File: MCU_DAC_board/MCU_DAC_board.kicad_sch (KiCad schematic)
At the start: 46 parts, among them J10 Conn_01x03_Pin, J11 105-0752-001, J12 Conn_02x03_Odd_Even, J5 54-00127, J6 105-0752-001, J7 Screw_Terminal_01x02, J8 Screw_Terminal_01x02, J9 Conn_02x20_Odd_Even, Q1 FZT953, U1 ADAU1966AWBSTZ

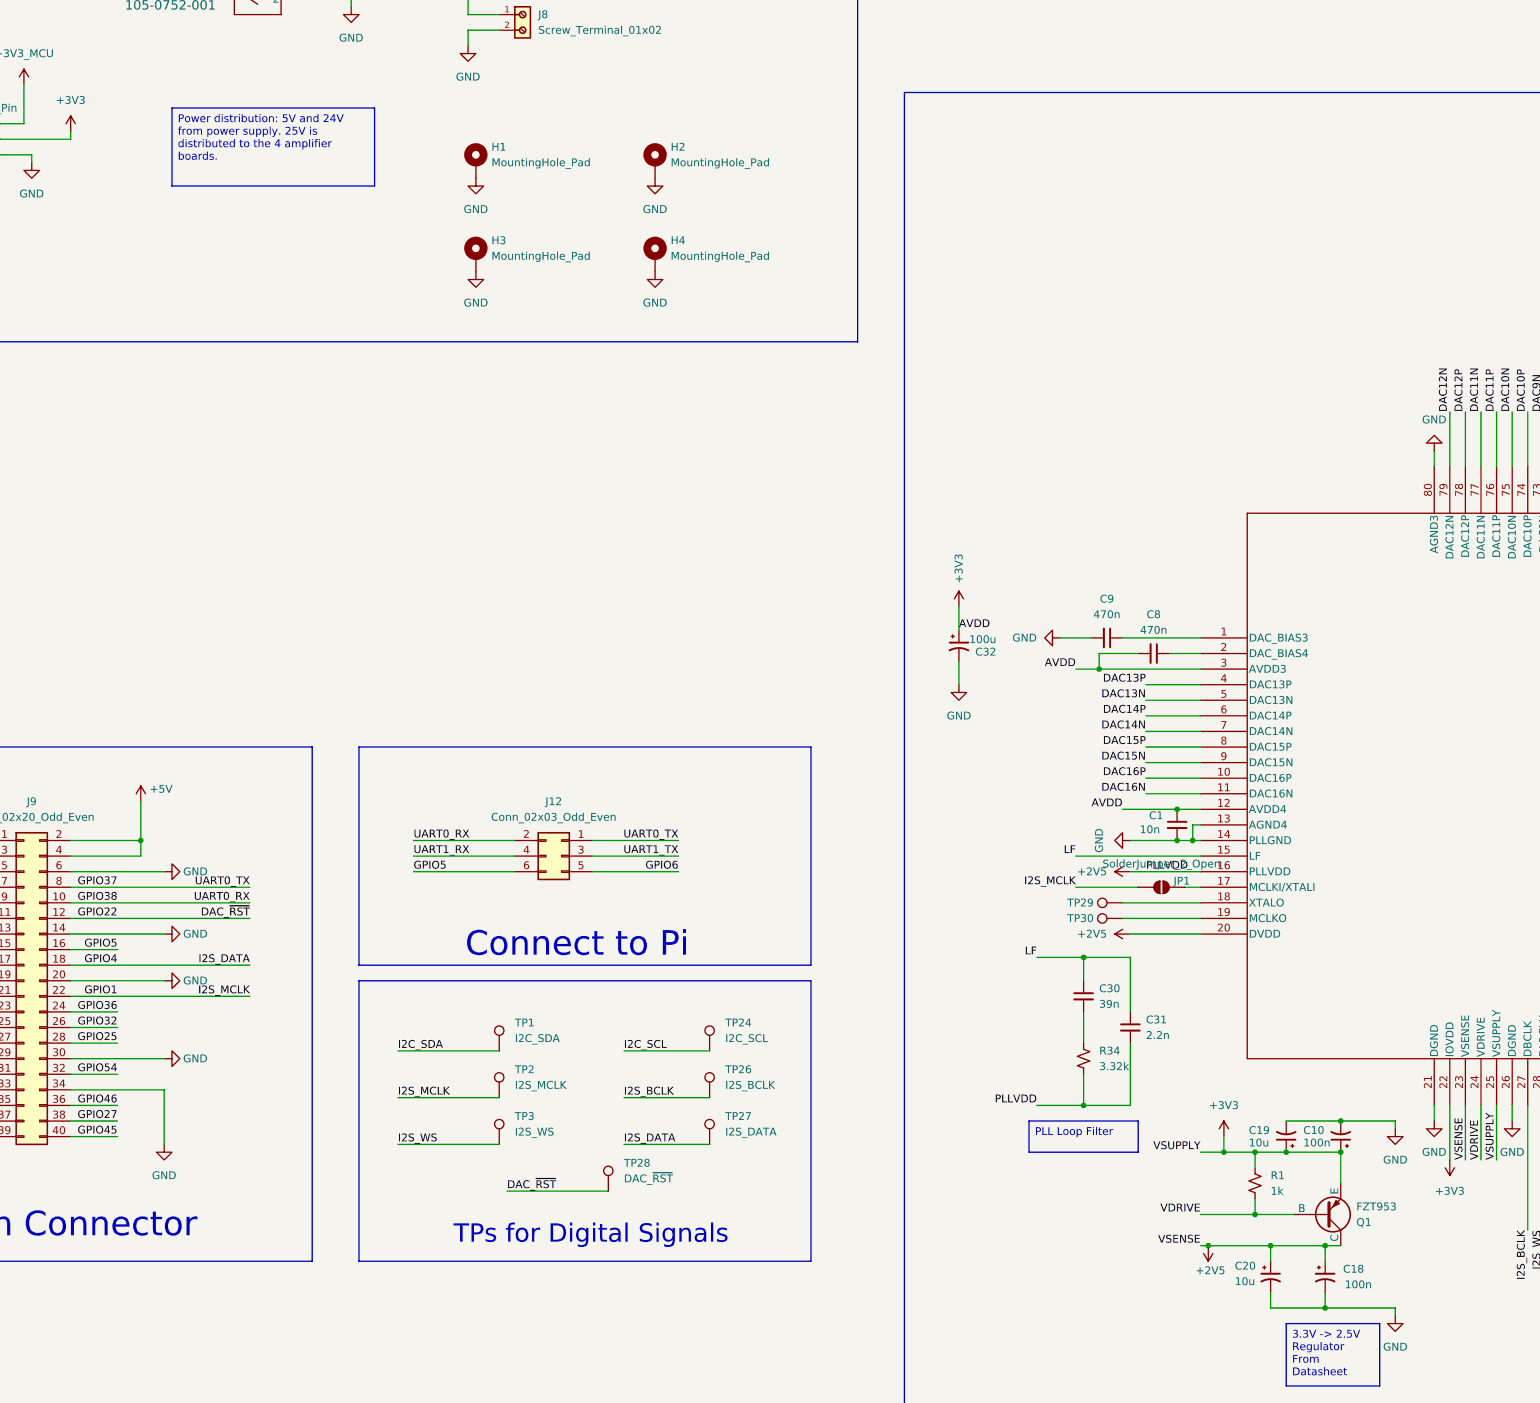
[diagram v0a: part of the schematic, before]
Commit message: First revision of DAC board
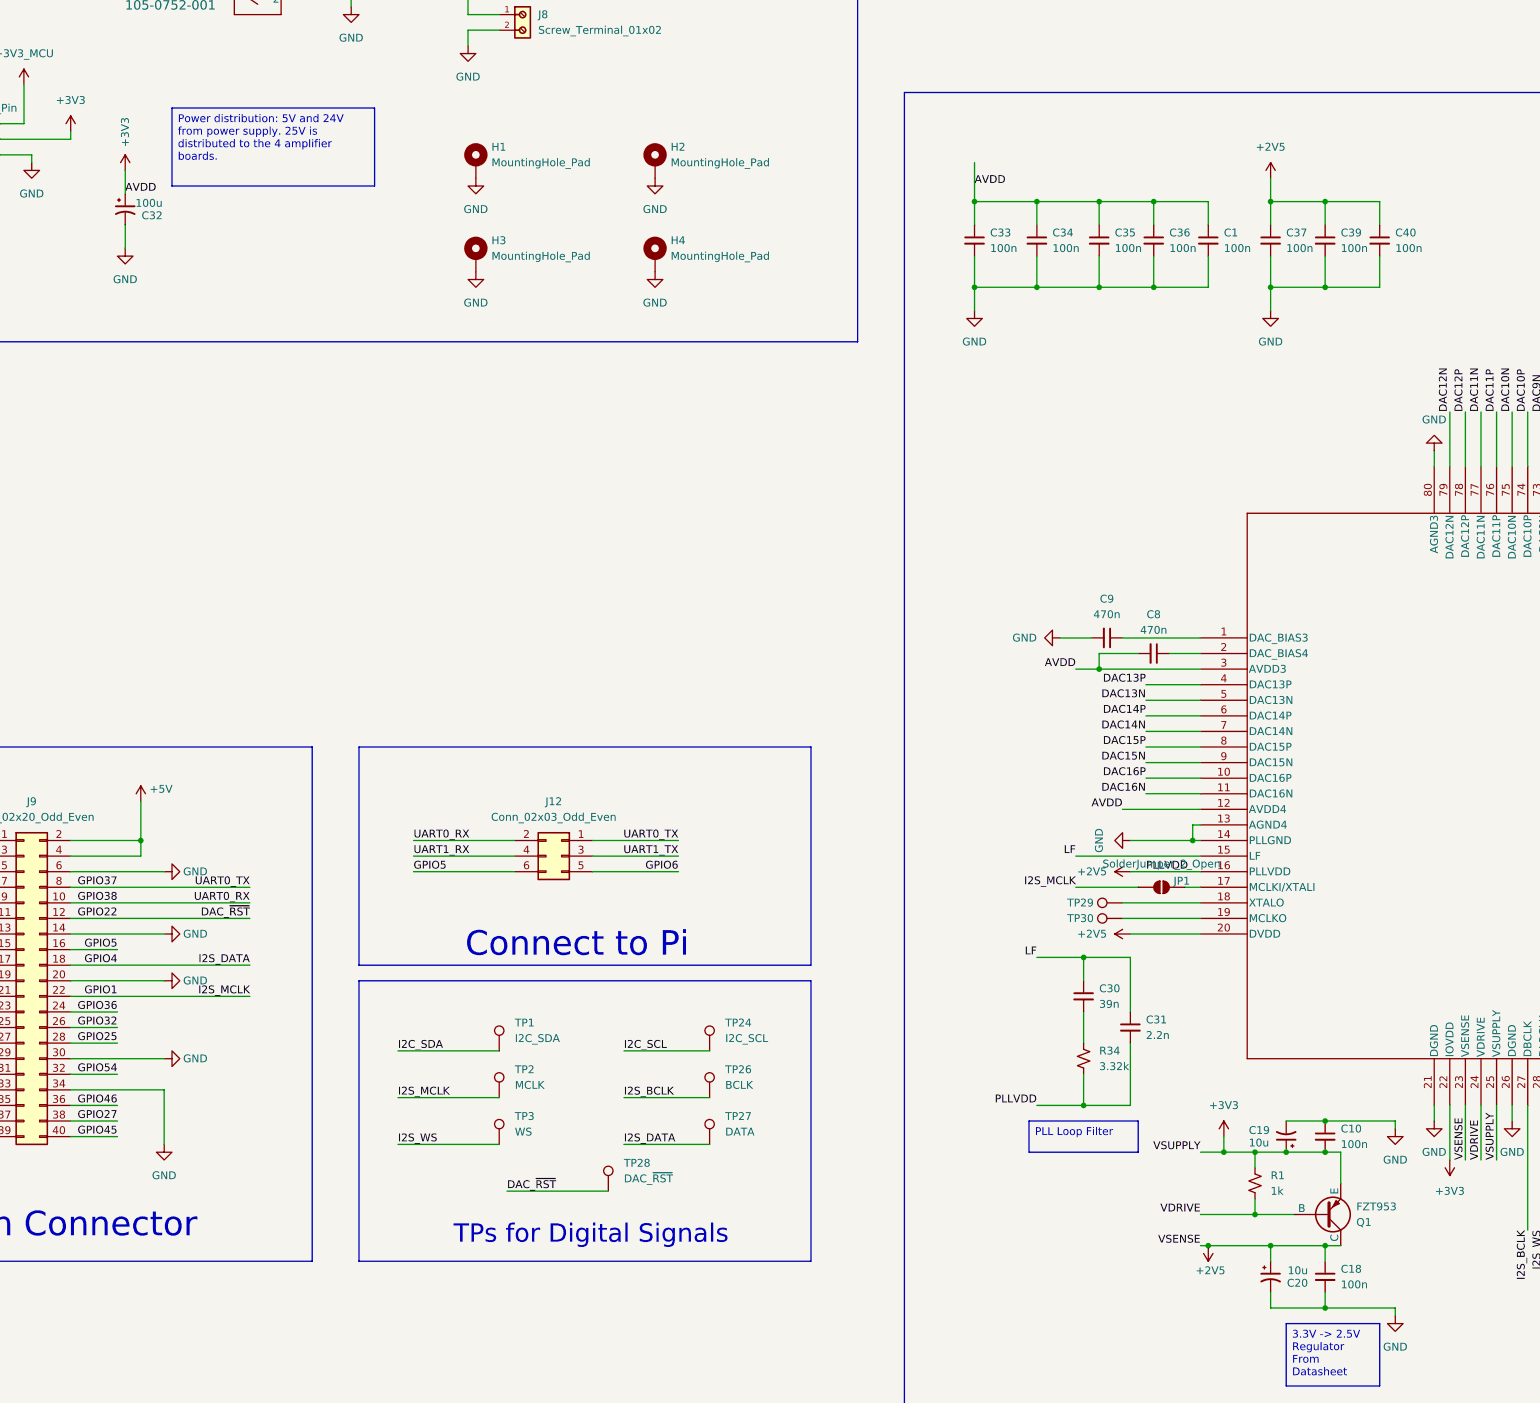
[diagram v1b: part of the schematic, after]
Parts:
- removed C10, C18: 100n, Capacitor_SMD:C_0805_2012Metric_Pad1.18x1.45mm_HandSolder, symbol Device:C_Polarized_Small_US
- added C10, C18, C33, C34, C35, C36, C37, C39, C40: 100n, Capacitor_SMD:C_0603_1608Metric_Pad1.08x0.95mm_HandSolder, symbol Device:C_Small
- C1: value 10n -> 100n; footprint Capacitor_SMD:C_0805_2012Metric_Pad1.18x1.45mm_HandSolder -> Capacitor_SMD:C_0603_1608Metric_Pad1.08x0.95mm_HandSolder
- C19, C20: footprint Capacitor_SMD:C_0805_2012Metric_Pad1.18x1.45mm_HandSolder -> Capacitor_SMD:CP_Elec_4x4.5
- C2, C3, C4, C7, C8, C9: footprint Capacitor_SMD:C_0805_2012Metric_Pad1.18x1.45mm_HandSolder -> Capacitor_SMD:C_0603_1608Metric_Pad1.08x0.95mm_HandSolder
- TP2: value I2S_MCLK -> MCLK
- TP26: value I2S_BCLK -> BCLK
- TP27: value I2S_DATA -> DATA
- TP3: value I2S_WS -> WS
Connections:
- net +2V5: now also C18.1, C37.1, C39.1, C40.1
- net +3V3: now also C10.2, C33.1, C34.1, C35.1, C36.1
- net GND: now also C10.1, C18.2, C33.2, C34.2, C35.2, C36.2, C37.2, C39.2, C40.2
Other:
- moved on the sheet: C32

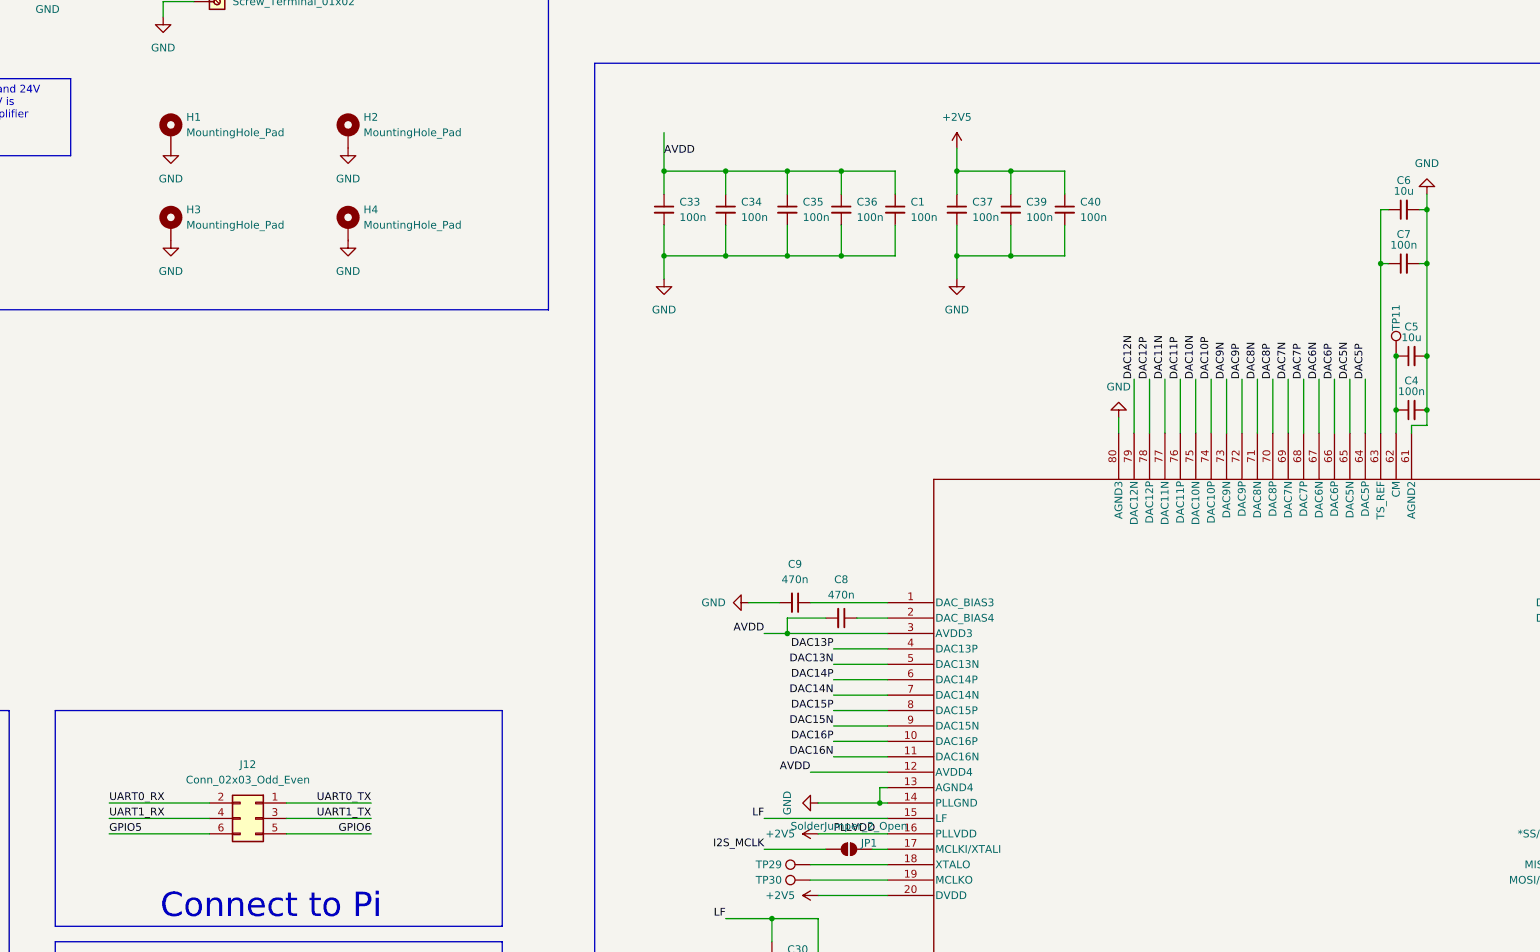
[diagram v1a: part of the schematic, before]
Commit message: Added via stiching, more decoupling
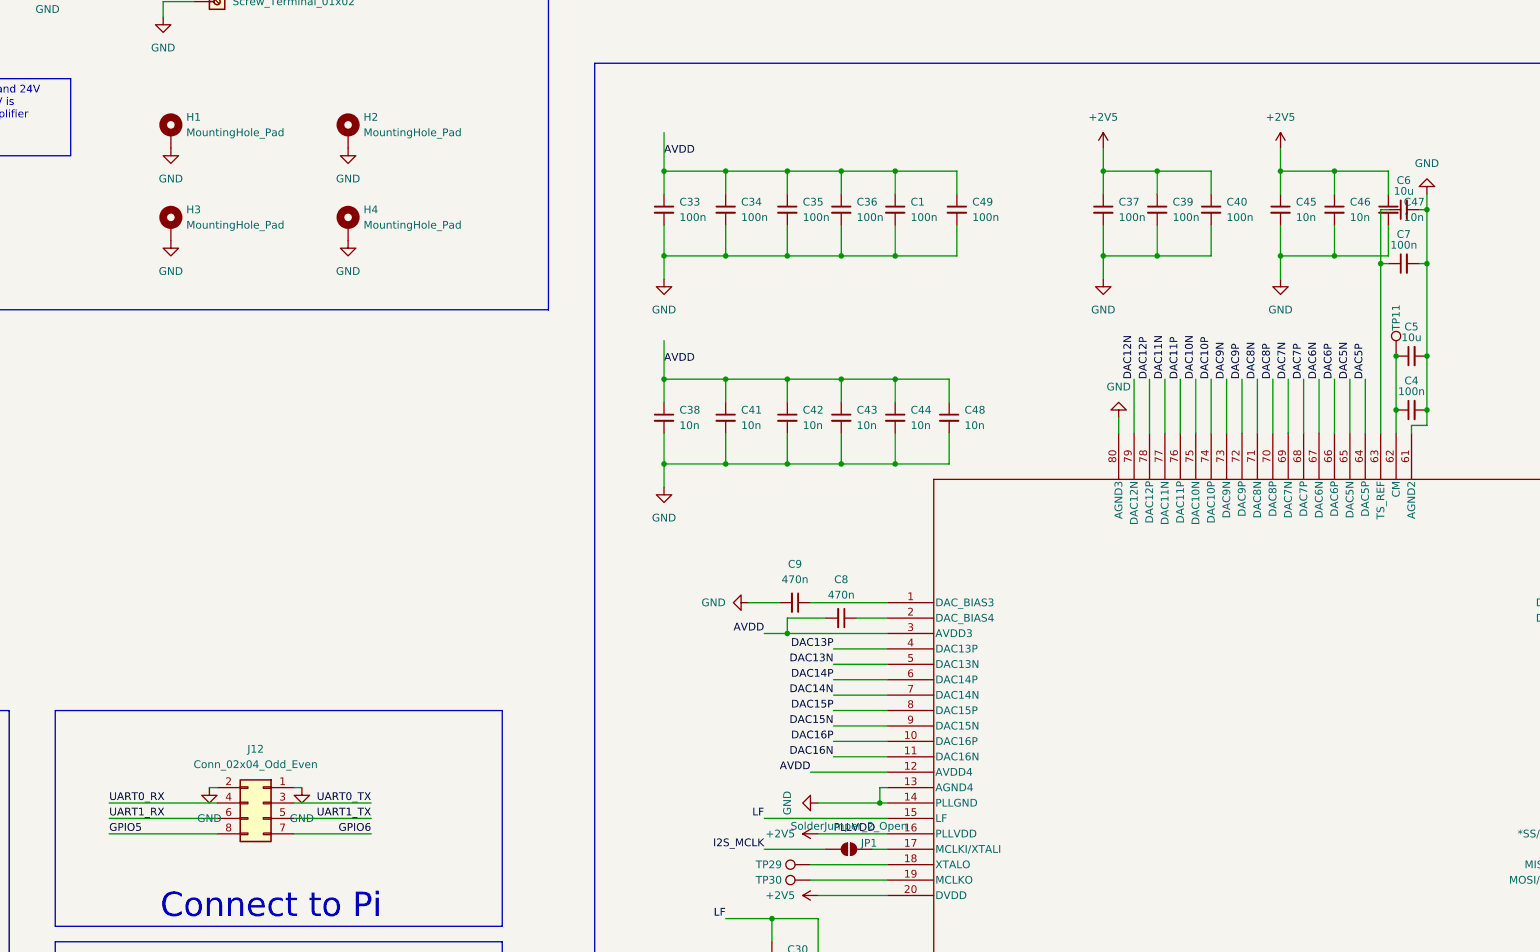
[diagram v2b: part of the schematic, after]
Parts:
- removed J12: Conn_02x03_Odd_Even, Connector_PinSocket_2.54mm:PinSocket_2x03_P2.54mm_Vertical, symbol Connector_Generic:Conn_02x03_Odd_Even
- added C38, C41, C42, C43, C44, C45, C46, C47, C48: 10n, Capacitor_SMD:C_0603_1608Metric_Pad1.08x0.95mm_HandSolder, symbol Device:C_Small
- added C49: 100n, Capacitor_SMD:C_0603_1608Metric_Pad1.08x0.95mm_HandSolder, symbol Device:C_Small
- added J12: Conn_02x04_Odd_Even, Connector_PinSocket_2.54mm:PinSocket_2x04_P2.54mm_Vertical, symbol Connector_Generic:Conn_02x04_Odd_Even
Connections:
- net +2V5: now also C45.1, C46.1, C47.1
- net +3V3: now also C38.1, C41.1, C42.1, C43.1, C44.1, C48.1, C49.1
- net GND: now also C38.2, C41.2, C42.2, C43.2, C44.2, C45.2, C46.2, C47.2, C48.2, C49.2, J12.1 (Pin_1), J12.2 (Pin_2)
- net GPIO20: now also J12.5 (Pin_5)
- net GPIO21: now also J12.6 (Pin_6)
- net GPIO37: now also J12.3 (Pin_3)
- net GPIO38: now also J12.4 (Pin_4)
- net GPIO5: now also J12.8 (Pin_8)
- net GPIO6: now also J12.7 (Pin_7)
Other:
- moved on the sheet: C37, C39, C40
